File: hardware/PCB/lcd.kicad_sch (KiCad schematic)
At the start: 11 parts, among them U1 TSC2013QRSARQ1, U2 BCR421UW6-7

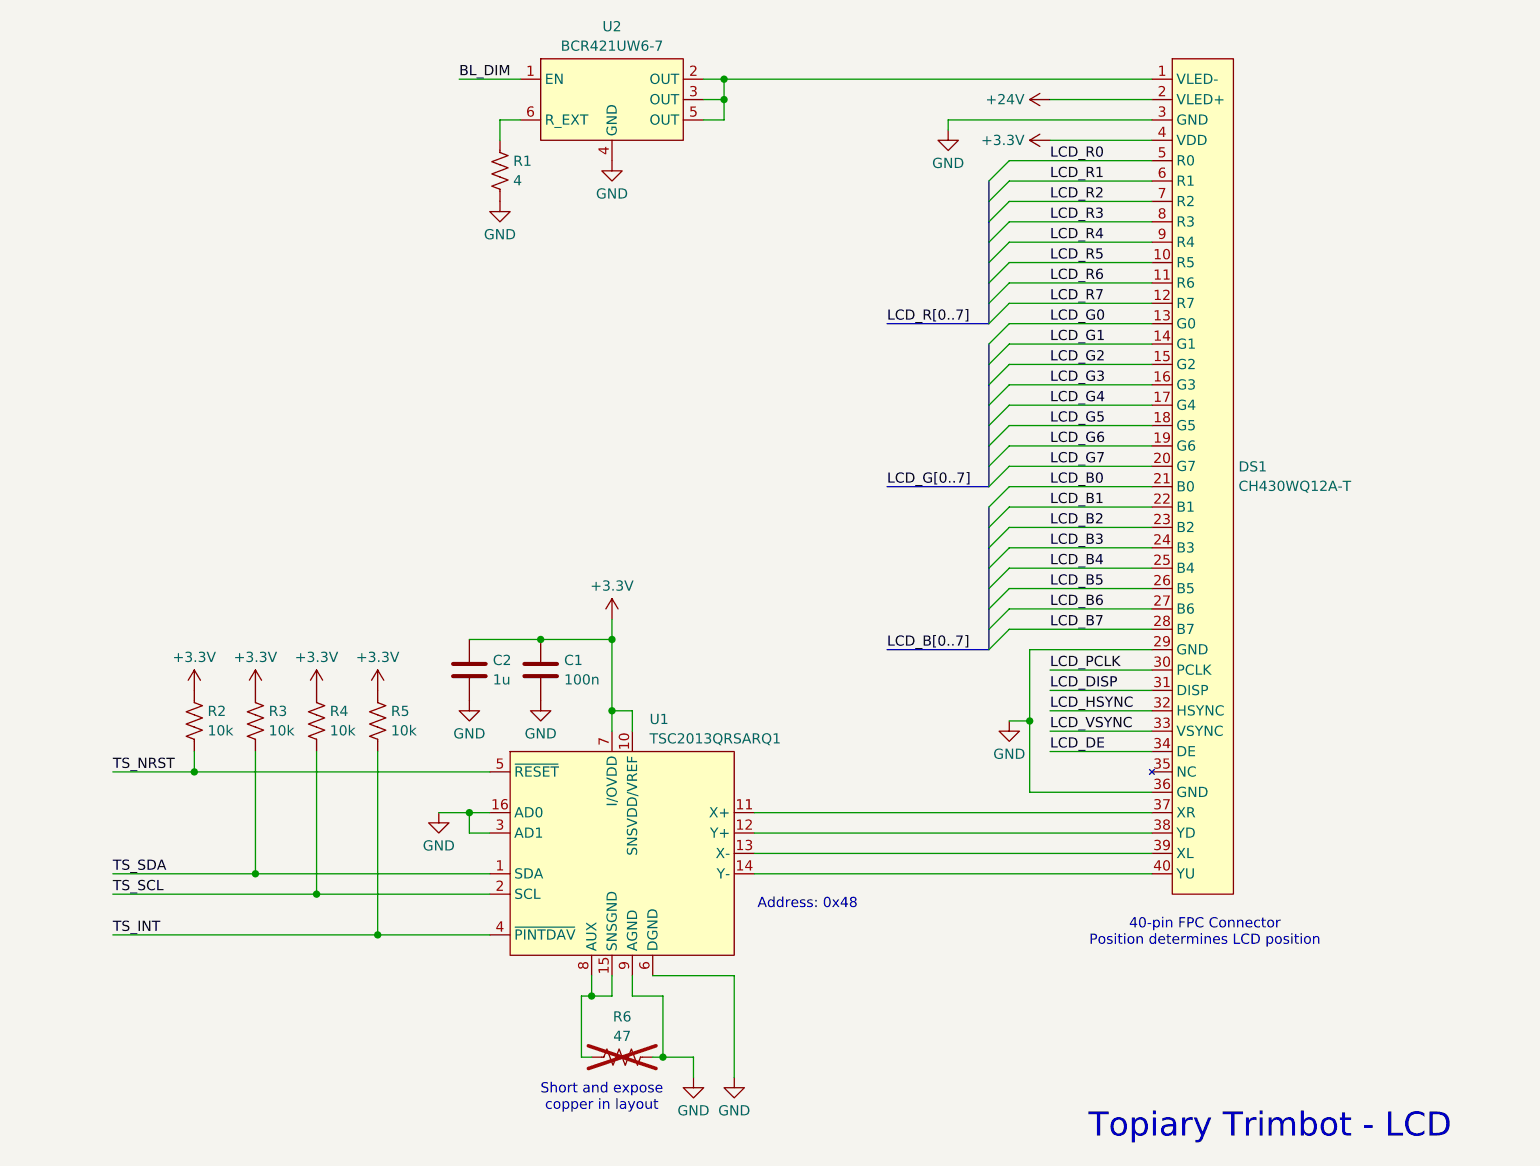
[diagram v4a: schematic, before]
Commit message: Schematic: minor changes to lcd
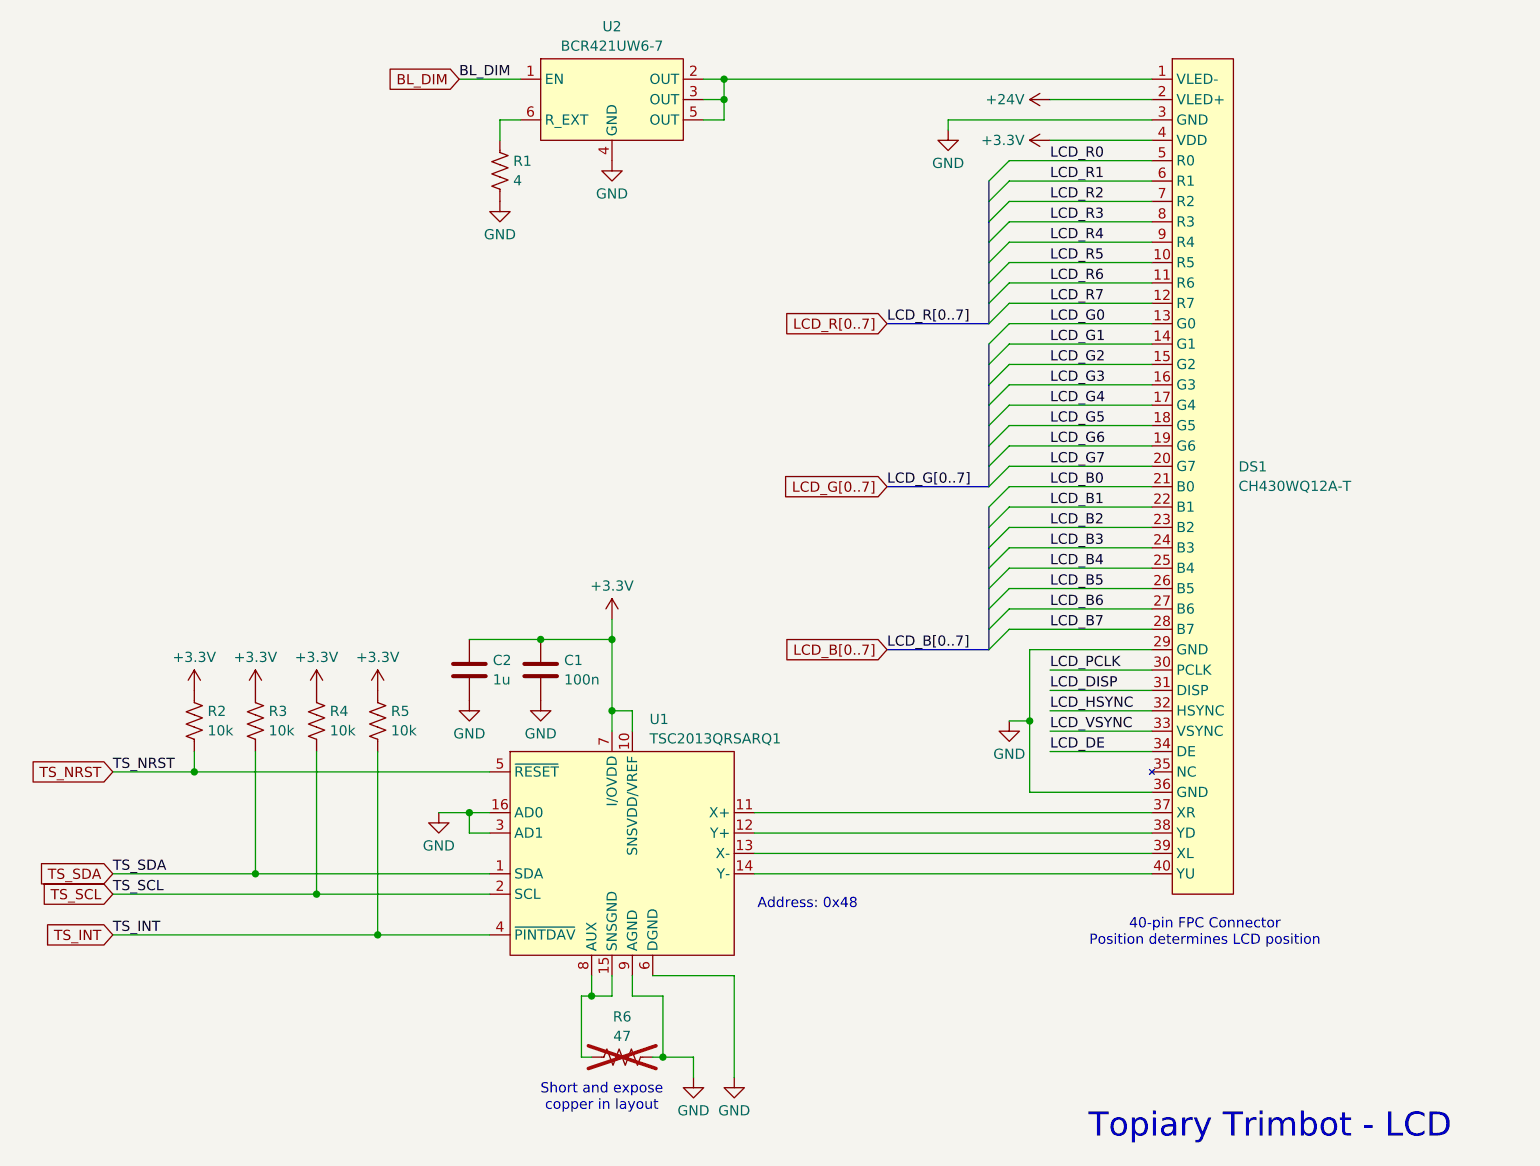
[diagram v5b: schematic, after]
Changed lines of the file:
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@@
+		)
+	)
+	(global_label "TS_NRST"
+		(shape input)
+		(at 63.5 129.54 180)
+		(fields_autoplaced yes)
+		(effects
+			(font
+				(size 1.27 1.27)
+			)
+			(justify right)
+		)
+		(property "Intersheetrefs" "${INTERSHEET_REFS}"
+			(at 52.5925 129.54 0)
+			(effects
+				(font
+					(size 1.27 1.27)
+				)
+				(justify right)
+				(hide yes)
+			)
+		)
+	)
+	(global_label "LCD_R[0..7]"
+		(shape input)
+		(at 160.02 73.66 180)
+		(fields_autoplaced yes)
+		(effects
+			(font
+				(size 1.27 1.27)
+			)
+			(justify right)
+		)
+		(property "Intersheetrefs" "${INTERSHEET_REFS}"
+			(at 145.9071 73.66 0)
+			(effects
+				(font
+					(size 1.27 1.27)
+				)
+				(justify right)
+				(hide yes)
+			)
+		)
+	)
+	(global_label "TS_SDA"
+		(shape input)
+		(at 63.5 142.24 180)
+		(fields_autoplaced yes)
+		(effects
+			(font
+				(size 1.27 1.27)
+			)
+			(justify right)
+		)
+		(property "Intersheetrefs" "${INTERSHEET_REFS}"
+			(at 53.802 142.24 0)
+			(effects
+				(font
+					(size 1.27 1.27)
+				)
+				(justify right)
+				(hide yes)
+			)
+		)
+	)
+	(global_label "LCD_B[0..7]"
+		(shape input)
+		(at 160.02 114.3 180)
+		(fields_autoplaced yes)
+		(effects
+			(font
+				(size 1.27 1.27)
+			)
+			(justify right)
+		)
+		(property "Intersheetrefs" "${INTERSHEET_REFS}"
+			(at 145.9071 114.3 0)
+			(effects
+				(font
+					(size 1.27 1.27)
+				)
+				(justify right)
+				(hide yes)
+			)
+		)
+	)
+	(global_label "LCD_G[0..7]"
+		(shape input)
+		(at 160.02 93.98 180)
+		(fields_autoplaced yes)
+		(effects
+			(font
+				(size 1.27 1.27)
+			)
+			(justify right)
+		)
+		(property "Intersheetrefs" "${INTERSHEET_REFS}"
+			(at 145.9071 93.98 0)
+			(effects
+				(font
+					(size 1.27 1.27)
+				)
+				(justify right)
+				(hide yes)
+			)
+		)
+	)
+	(global_label "TS_INT"
+		(shape input)
+		(at 63.5 149.86 180)
+		(fields_autoplaced yes)
+		(effects
+			(font
+				(size 1.27 1.27)
+			)
+			(justify right)
+		)
+		(property "Intersheetrefs" "${INTERSHEET_REFS}"
+			(at 54.4672 149.86 0)
+			(effects
+				(font
+					(size 1.27 1.27)
+				)
+				(justify right)
+				(hide yes)
+			)
+		)
+	)
+	(global_label "TS_SCL"
+		(shape input)
+		(at 63.5 144.78 180)
+		(fields_autoplaced yes)
+		(effects
+			(font
+				(size 1.27 1.27)
+			)
+			(justify right)
+		)
+		(property "Intersheetrefs" "${INTERSHEET_REFS}"
+			(at 53.8625 144.78 0)
+			(effects
+				(font
+					(size 1.27 1.27)
+				)
+				(justify right)
+				(hide yes)
+			)
+		)
+	)
+	(global_label "BL_DIM"
+		(shape input)
+		(at 106.68 43.18 180)
+		(fields_autoplaced yes)
+		(effects
+			(font
+				(size 1.27 1.27)
+			)
+			(justify right)
+		)
+		(property "Intersheetrefs" "${INTERSHEET_REFS}"
+			(at 97.1029 43.18 0)
+			(effects
+				(font
+					(size 1.27 1.27)
+				)
+				(justify right)
+				(hide yes)
+			)
 		)
 	)
